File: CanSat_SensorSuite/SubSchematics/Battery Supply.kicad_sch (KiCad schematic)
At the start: 11 parts, among them J4 XT30_THT_H, U4 NCP1117_3.3

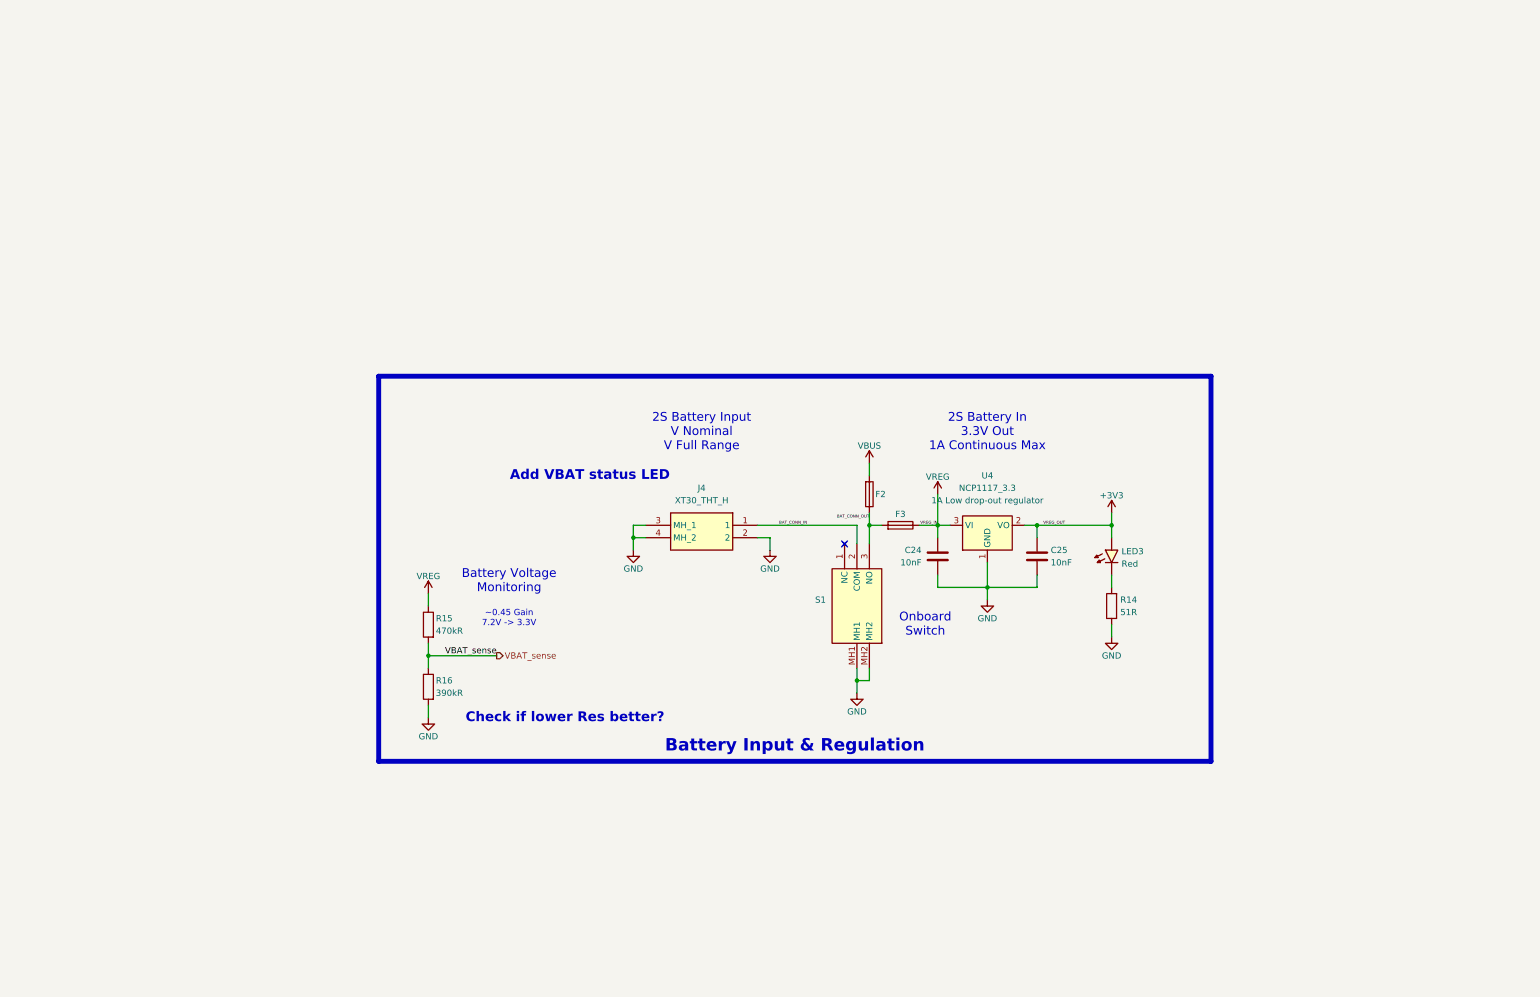
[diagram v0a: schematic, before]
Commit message: Minor schematic changes
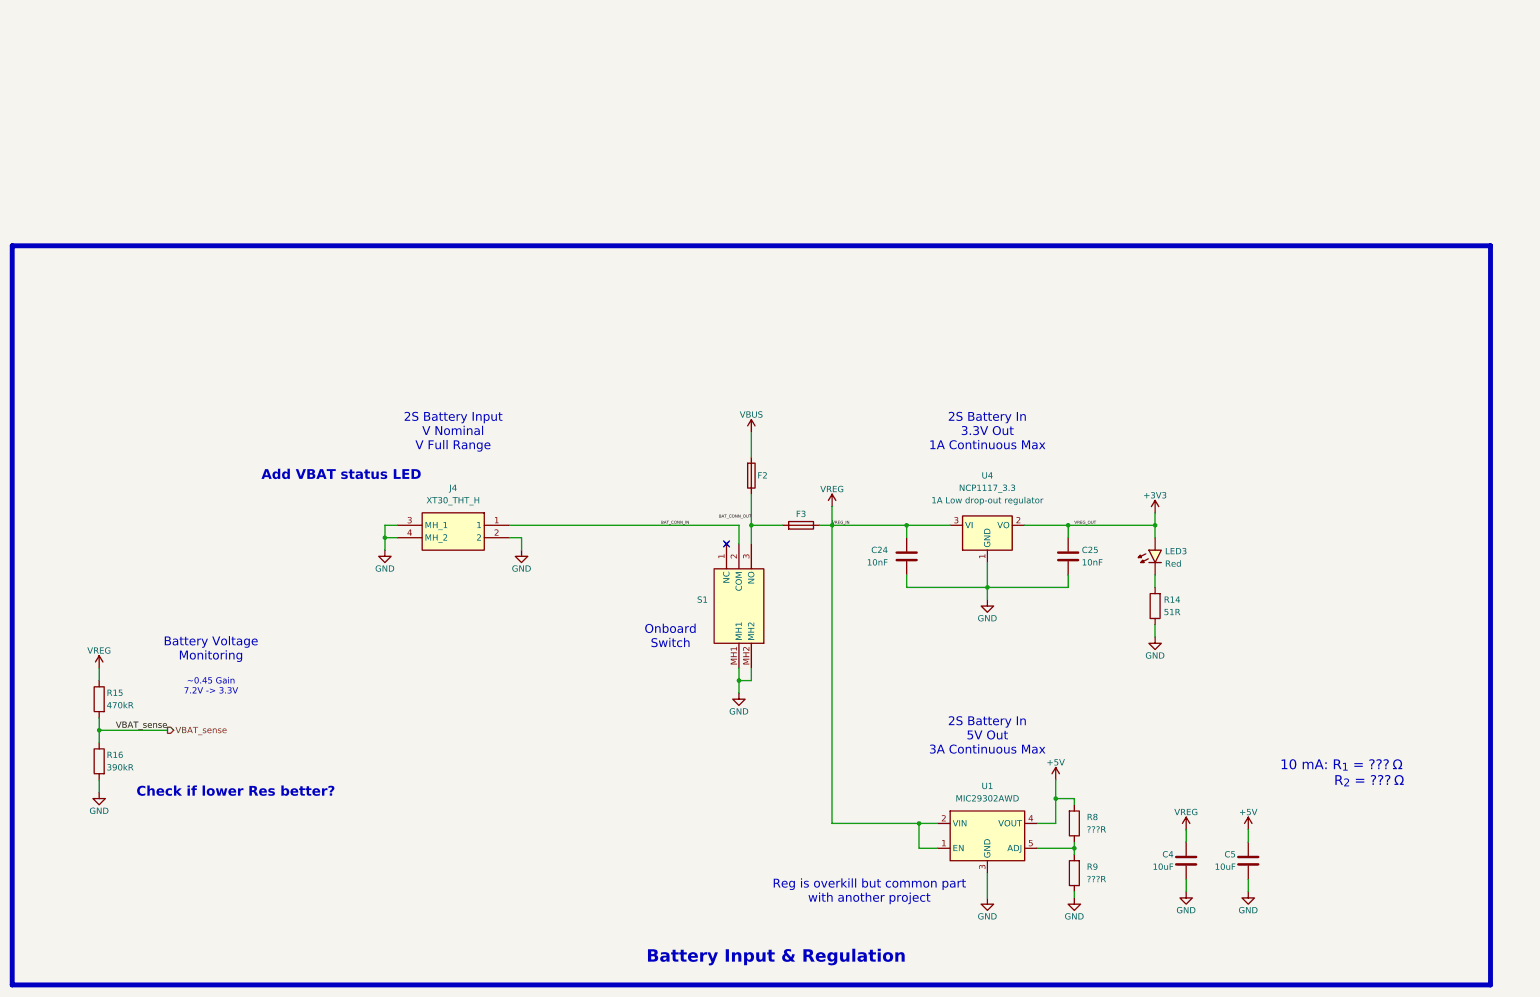
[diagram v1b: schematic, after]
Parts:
- added C4, C5: 10uF, 0_Capacitors:C_0603_1608_DensityHigh, symbol 0_Passives:C
- added R8, R9: ???R, 0_Resistors:R_0603_1608_DensityHigh, symbol 0_Passives:R
- added U1: MIC29302AWD, 0_Power:TO-252-5_TabPin3, symbol 0_Power:MIC29302AWD
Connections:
- net GND: now also C4.2, C5.2, R9.2, U1.3 (GND)
- net VREG: now also C4.1, U1.1 (EN), U1.2 (VIN)
- new net: R8.2, R9.1, U1.5 (ADJ)
- new net +5V: C5.1, R8.1, U1.4 (VOUT)
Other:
- note added: "10 mA: R_{1} = ??? Ω R_{2} = ??? Ω"
- note added: "2S Battery In 5V Out 3A Continuous Max"
- note added: "Reg is overkill but common part with another project"
- moved on the sheet: C24, C25, F2, F3, J4, LED3, R14, R15, R16, S1

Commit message: Example files update
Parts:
- renumbered C4 to C26, C5 to C27, LED3 to LED4, R14 to R15, R8 to R16, R9 to R17, R15 to R18, R16 to R19, U1 to U5
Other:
- note removed: "Reg is overkill but common part with another project"
- company: (none) -> ${COMPANY}
- title: (none) -> Battery Supply & Regulation

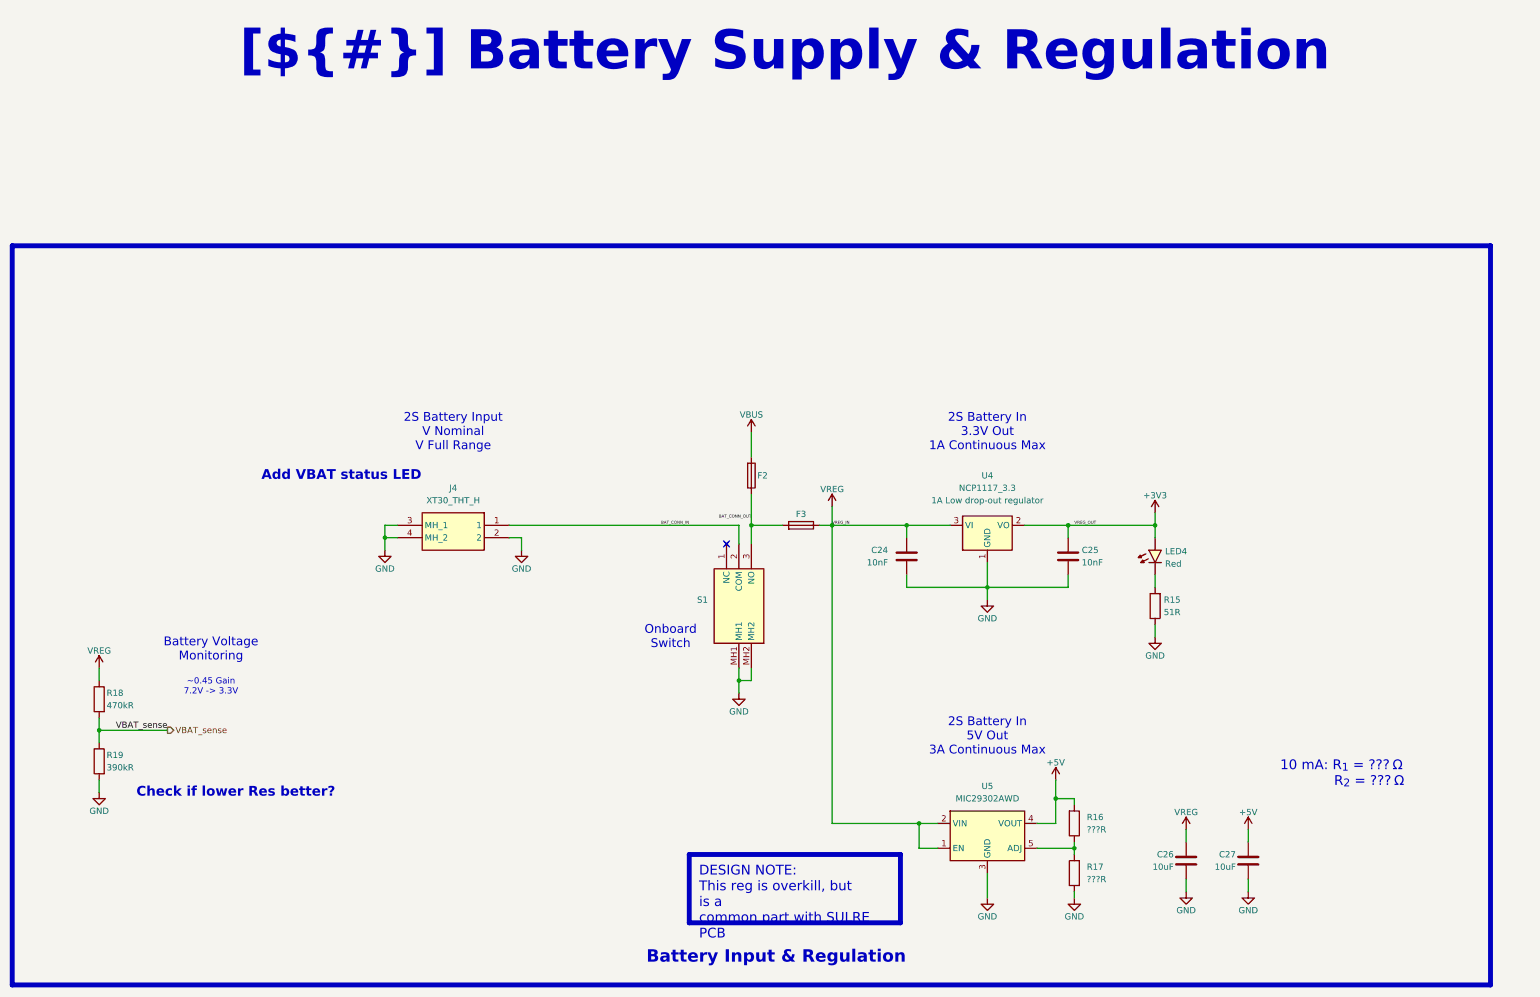
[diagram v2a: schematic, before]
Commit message: Minor schematic changes
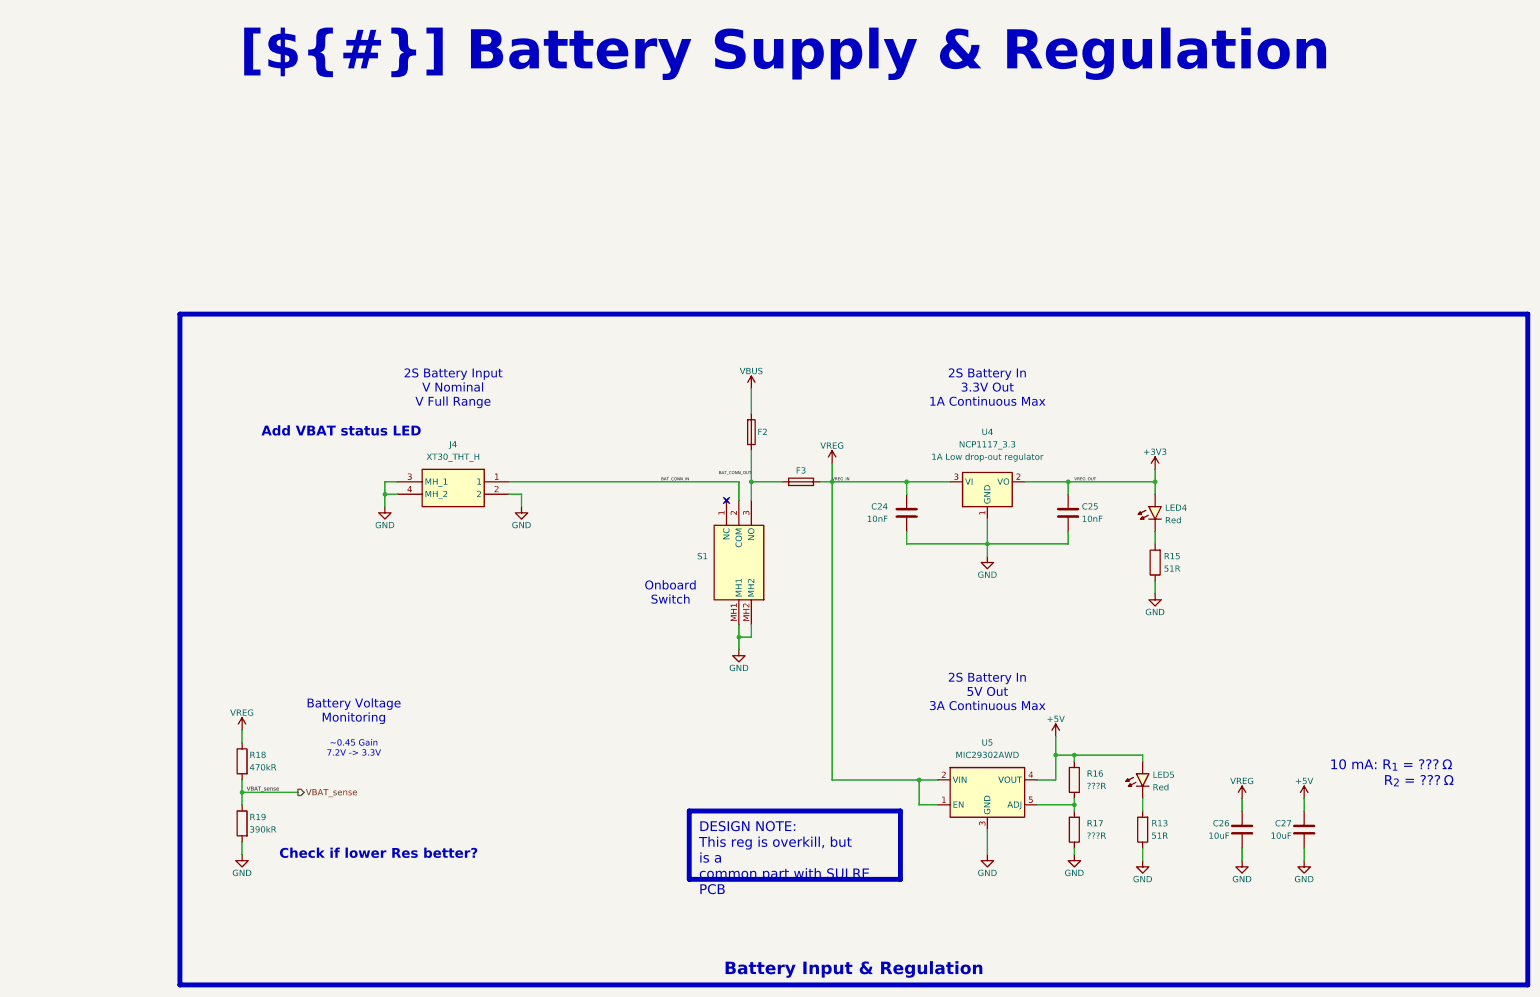
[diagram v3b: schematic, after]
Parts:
- added LED5: Red, 0_Passives:LED_0603_1608Metric, symbol 0_Passives:LED_R
- added R13: 51R, 0_Resistors:R_0603_1608_DensityHigh, symbol 0_Passives:R
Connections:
- net +5V: now also LED5.2 (A)
- net GND: now also R13.2
- new net: LED5.1 (K), R13.1
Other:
- moved on the sheet: C24, C25, C26, C27, F2, F3, J4, LED4, R15, R16, R17, R18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
